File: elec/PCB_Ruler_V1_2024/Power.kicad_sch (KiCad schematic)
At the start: 0 parts

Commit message: battery charger
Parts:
- added C5, C6: 4.7uF, symbol Device:C
- added D1: LED_Small, symbol Device:LED_Small
- added R3: 2k, symbol Device:R
- added R4: 470, symbol Device:R
- added U1: MCP73831T-2ACI_OT, digikey-footprints:SOT-753, symbol dk_PMIC-Battery-Chargers:MCP73831T-2ACI_OT
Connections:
- new net: R4.2, U1.1 (STAT)
- new net: R3.1, U1.5 (PROG)
- new net: D1.1 (K), R4.1
- new net +5V: C6.1, D1.2 (A), U1.4 (VDD)
- new net GND: C5.2, C6.2, R3.2, U1.2 (VSS)
- new net Vbat+: C5.1, U1.3 (VBAT)

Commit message: this is for my strong girl
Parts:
- added U3: TLV75533PDBV, Package_TO_SOT_SMD:SOT-23-5, symbol Regulator_Linear:TLV75533PDBV
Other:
- moved on the sheet: C5
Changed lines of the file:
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@@
 	(wire
 		(pts
-			(xy 168.91 46.99) (xy 176.53 46.99)
+			(xy 139.7 53.34) (xy 147.32 53.34)
 		)
 		(stroke
@@
 	(wire
 		(pts
-			(xy 176.53 57.15) (xy 176.53 58.42)
+			(xy 147.32 63.5) (xy 147.32 64.77)
 		)
 		(stroke
@@
 	(wire
 		(pts
-			(xy 176.53 46.99) (xy 176.53 49.53)
+			(xy 147.32 53.34) (xy 147.32 55.88)
 		)
 		(stroke
@@
 	(global_label "Vbat+"
 		(shape input)
-		(at 168.91 46.99 180)
+		(at 139.7 53.34 180)
 		(fields_autoplaced yes)
 		(effects
@@
 		)
 		(property "Intersheetrefs" "${INTERSHEET_REFS}"
-			(at 160.2401 46.99 0)
+			(at 131.0301 53.34 0)
 			(effects
 				(font
@@
 	(symbol
 		(lib_id "Device:C")
-		(at 176.53 53.34 0)
+		(at 147.32 59.69 0)
 		(unit 1)
 		(exclude_from_sim no)
@@
 		(fields_autoplaced yes)
 		(property "Reference" "C5"
-			(at 180.34 52.0699 0)
+			(at 151.13 58.4199 0)
 			(effects
 				(font
@@
 		)
 		(property "Value" "4.7uF"
-			(at 180.34 54.6099 0)
+			(at 151.13 60.9599 0)
 			(effects
 				(font
@@
 		)
 		(property "Footprint" ""
-			(at 177.4952 57.15 0)
+			(at 148.2852 63.5 0)
 			(effects
 				(font
@@
 		)
 		(property "Datasheet" "~"
-			(at 176.53 53.34 0)
+			(at 147.32 59.69 0)
 			(effects
 				(font
@@
 		)
 		(property "Description" "Unpolarized capacitor"
-			(at 176.53 53.34 0)
+			(at 147.32 59.69 0)
 			(effects
 				(font
@@
 	)
 	(symbol
+		(lib_id "Regulator_Linear:TLV75533PDBV")
+		(at 199.39 62.23 0)
+		(unit 1)
+		(exclude_from_sim no)
+		(in_bom yes)
+		(on_board yes)
+		(dnp no)
+		(fields_autoplaced yes)
+		(property "Reference" "U3"
+			(at 199.39 53.34 0)
+			(effects
+				(font
+					(size 1.27 1.27)
+				)
+			)
+		)
+		(property "Value" "TLV75533PDBV"
+			(at 199.39 55.88 0)
+			(effects
+				(font
+					(size 1.27 1.27)
+				)
+			)
+		)
+		(property "Footprint" "Package_TO_SOT_SMD:SOT-23-5"
+			(at 199.39 53.975 0)
+			(effects
+				(font
+					(size 1.27 1.27)
+					(italic yes)
+				)
+				(hide yes)
+			)
+		)
+		(property "Datasheet" "http://www.ti.com/lit/ds/symlink/tlv755p.pdf"
+			(at 199.39 60.96 0)
+			(effects
+				(font
+					(size 1.27 1.27)
+				)
+				(hide yes)
+			)
+		)
+		(property "Description" "500mA Low Dropout Voltage Regulator, Fixed Output 3.3V, SOT-23-5"
+			(at 199.39 62.23 0)
+			(effects
+				(font
+					(size 1.27 1.27)
+				)
+				(hide yes)
+			)
+		)
+		(pin "2"
+		)
+		(pin "5"
+		)
+		(pin "1"
+		)
+		(pin "4"
+		)
+		(pin "3"
+		)
+		(instances
+			(project "PCB_Ruler_V1_2024"
+				(path "/e39575e5-bba1-47dc-9ccf-32a84e6da237/4bf8cdd1-6def-4ef5-937e-6e175da6cdd6"
+					(reference "U3")
+					(unit 1)
+				)
+			)
+		)
+	)
+	(symbol
 		(lib_id "Device:LED_Small")
 		(at 80.01 54.61 180)
@@
 	(symbol
 		(lib_id "power:GND")
-		(at 176.53 58.42 0)
+		(at 147.32 64.77 0)
 		(unit 1)
 		(exclude_from_sim no)
@@
 		(fields_autoplaced yes)
 		(property "Reference" "#PWR016"
-			(at 176.53 64.77 0)
+			(at 147.32 71.12 0)
 			(effects
 				(font
@@
 		)
 		(property "Value" "GND"
-			(at 176.53 63.5 0)
+			(at 147.32 69.85 0)
 			(effects
 				(font
@@
 		)
 		(property "Footprint" ""
-			(at 176.53 58.42 0)
+			(at 147.32 64.77 0)
 			(effects
 				(font
@@
 		)
 		(property "Datasheet" ""
-			(at 176.53 58.42 0)
+			(at 147.32 64.77 0)
 			(effects
 				(font
@@
 		)
 		(property "Description" "Power symbol creates a global label with name \"GND\" , ground"
-			(at 176.53 58.42 0)
-			(effects
-				(font
+			(at 147.32 64.77 0)
+			(effects
+				(font

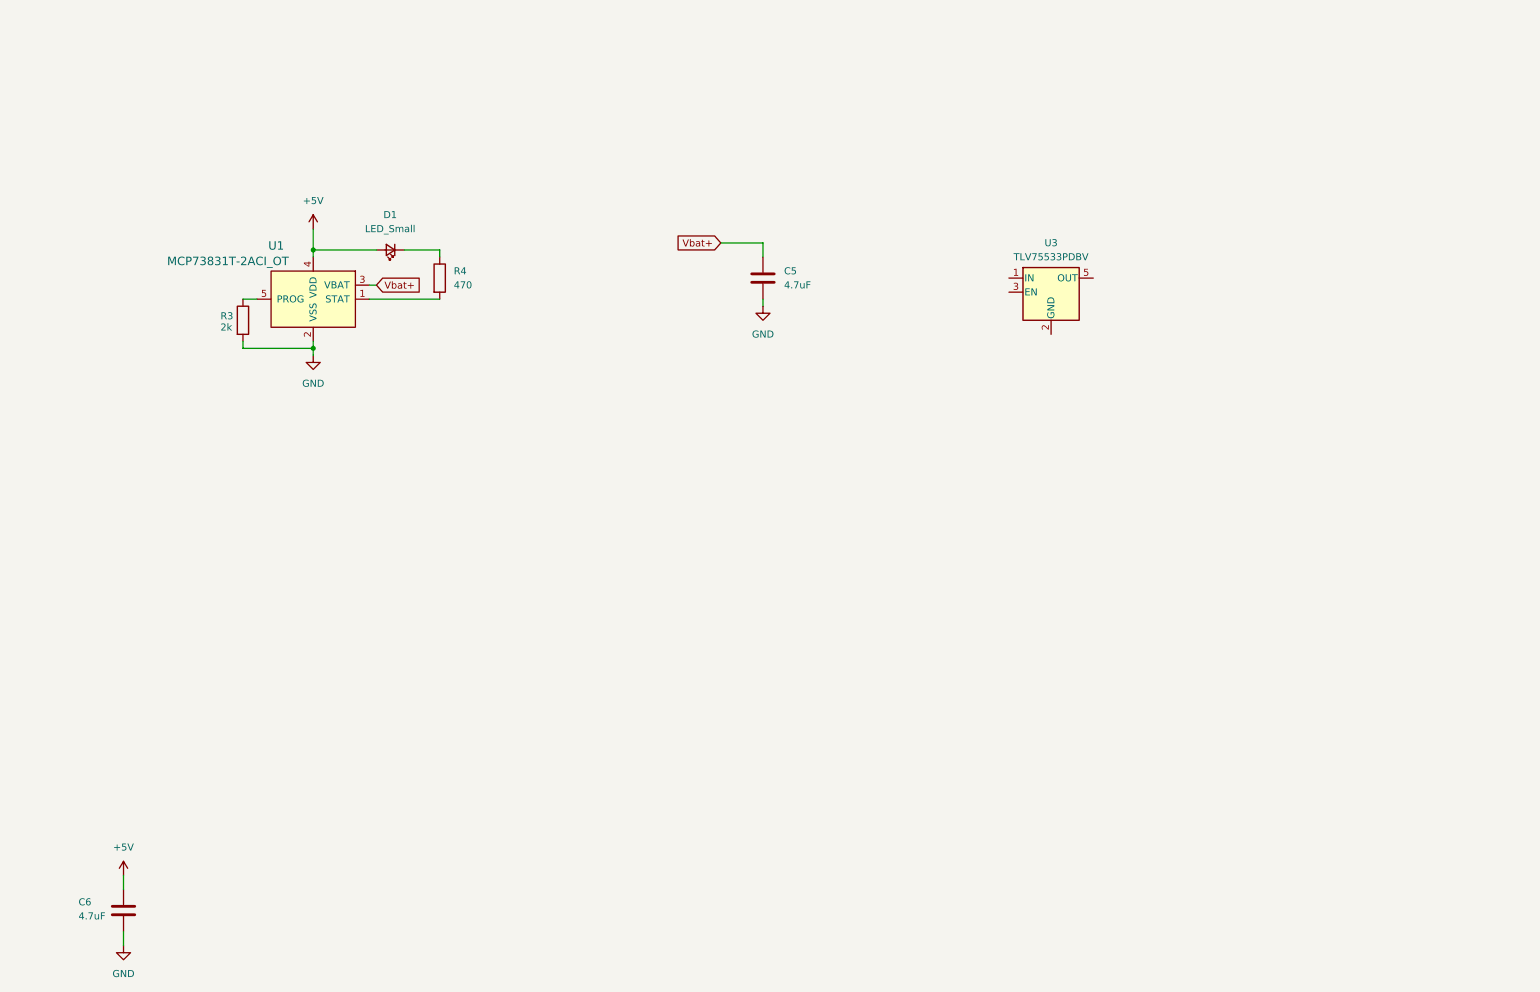
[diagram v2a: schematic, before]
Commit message: regulator 3V3
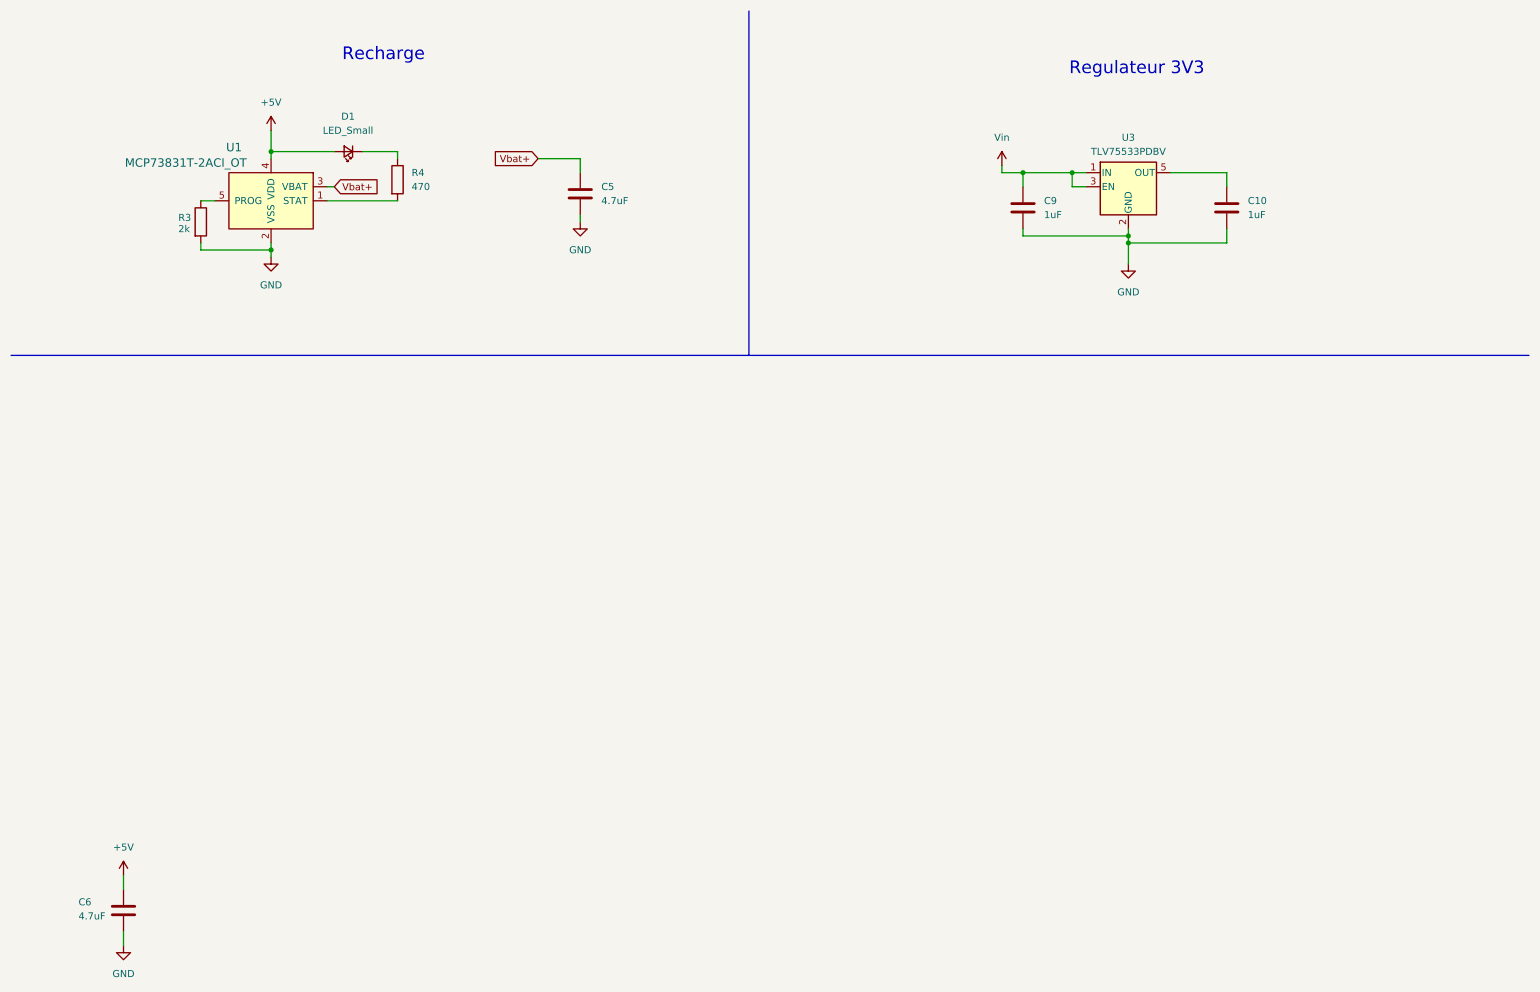
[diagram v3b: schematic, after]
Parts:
- added C10, C9: 1uF, symbol Device:C
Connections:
- net GND: now also U3.2 (GND), C10.2, C9.2
- net Vin: now reaches U3.1 (IN)
- net Vin: now also U3.3 (EN), C9.1
- net at U3.5 (OUT): now also C10.1
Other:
- note added: "Recharge"
- note added: "Regulateur 3V3"
- moved on the sheet: C5, D1, R3, R4, U1, U3

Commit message: Almost finished schematic...
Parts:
- added J3: S2B-XH-A-1LFSN, Connector_JST:JST_XH_S2B-XH-A-1_1x02_P2.50mm_Horizontal, symbol S2B-XH-A-1:S2B-XH-A-1LFSN
- added S1: JS202011JCQN, JS202011JCQN:SW_JS202011JCQN, symbol JS202011JCQN:JS202011JCQN
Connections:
- net GND: now also J3.2 (-)
- net Vbat+: now also J3.1 (+), S1.2, S1.6
- net +3V3: now reaches C10.1, U3.5 (OUT)
- net Vin: no longer names the net of C9.1, U3.1 (IN), U3.3 (EN)
- net Vin: now also S1.3, S1.7
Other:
- note added: "Header Batterie"
- moved on the sheet: C10, C5, C6, C9, D1, R3, R4, U1, U3

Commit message: started pcb
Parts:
- added R7: 100k, Resistor_SMD:R_0603_1608Metric_Pad0.98x0.95mm_HandSolder, symbol Device:R
- added R8: 300k, Resistor_SMD:R_0603_1608Metric_Pad0.98x0.95mm_HandSolder, symbol Device:R
- C3: renamed from C6; footprint (none) -> Capacitor_SMD:C_0603_1608Metric_Pad1.08x0.95mm_HandSolder
- C4: renamed from C5; footprint (none) -> Capacitor_SMD:C_0603_1608Metric_Pad1.08x0.95mm_HandSolder
- C5: renamed from C9; footprint (none) -> Capacitor_SMD:C_0603_1608Metric_Pad1.08x0.95mm_HandSolder
- C6: renamed from C10; footprint (none) -> Capacitor_SMD:C_0603_1608Metric_Pad1.08x0.95mm_HandSolder
- D3: renamed from D1; footprint (none) -> LED_SMD:LED_0603_1608Metric_Pad1.05x0.95mm_HandSolder
- R5: renamed from R4; footprint (none) -> Resistor_SMD:R_0603_1608Metric_Pad0.98x0.95mm_HandSolder
- R6: renamed from R3; footprint (none) -> Resistor_SMD:R_0603_1608Metric_Pad0.98x0.95mm_HandSolder
- renumbered J3 to J2, U1 to U2
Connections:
- net GND: now also R8.2
- net Vin: now reaches C5.1, S1.3, S1.7, U3.1 (IN), U3.3 (EN)
- net Vin: now also R7.1
- new net Val_Bat: R7.2, R8.1
- no-connect marks 0 -> 2
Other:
- note added: "Valeur Battery"

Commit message: started the pcb
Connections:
- net +3V3 renamed +3.3V

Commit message: coucou v2
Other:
- company: (none) -> FRANK_LAU
- title: (none) -> POWER_RULER 2024
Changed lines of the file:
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@@
 	(generator_version "8.0")
 	(paper "A4")
+	(title_block
+		(title "POWER_RULER 2024")
+		(date "2024-12-27")
+		(rev "A")
+		(company "FRANK_LAU")
+	)
 	(junction
 		(at 220.98 40.64)
